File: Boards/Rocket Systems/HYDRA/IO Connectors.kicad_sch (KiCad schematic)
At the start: 0 parts

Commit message: IO connectors
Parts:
- added DSUB1: ~, HDL15-SL-B:HDL15-SL-B, symbol HDL15-SL-B:HDL15-SL-B
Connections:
- new net ACT_N2 OUT: DSUB1.14
- new net ACT_N2 PWR: DSUB1.15
- new net ACT_N2O OUT: DSUB1.10
- new net ACT_N2O PWR: DSUB1.11
- new net Extra Valve OUT: DSUB1.2
- new net Extra Valve PWR: DSUB1.3
- new net GND: DSUB1.1
- new net QuickDisco N2 OUT: DSUB1.6
- new net QuickDisco N2 PWR: DSUB1.7
- new net QuickDisco N2O OUT: DSUB1.4
- new net QuickDisco N2O PWR: DSUB1.5
- new net VENT_N2 OUT: DSUB1.12
- new net VENT_N2 PWR: DSUB1.13
- new net VENT_N2O OUT: DSUB1.8
- new net VENT_N2O PWR: DSUB1.9

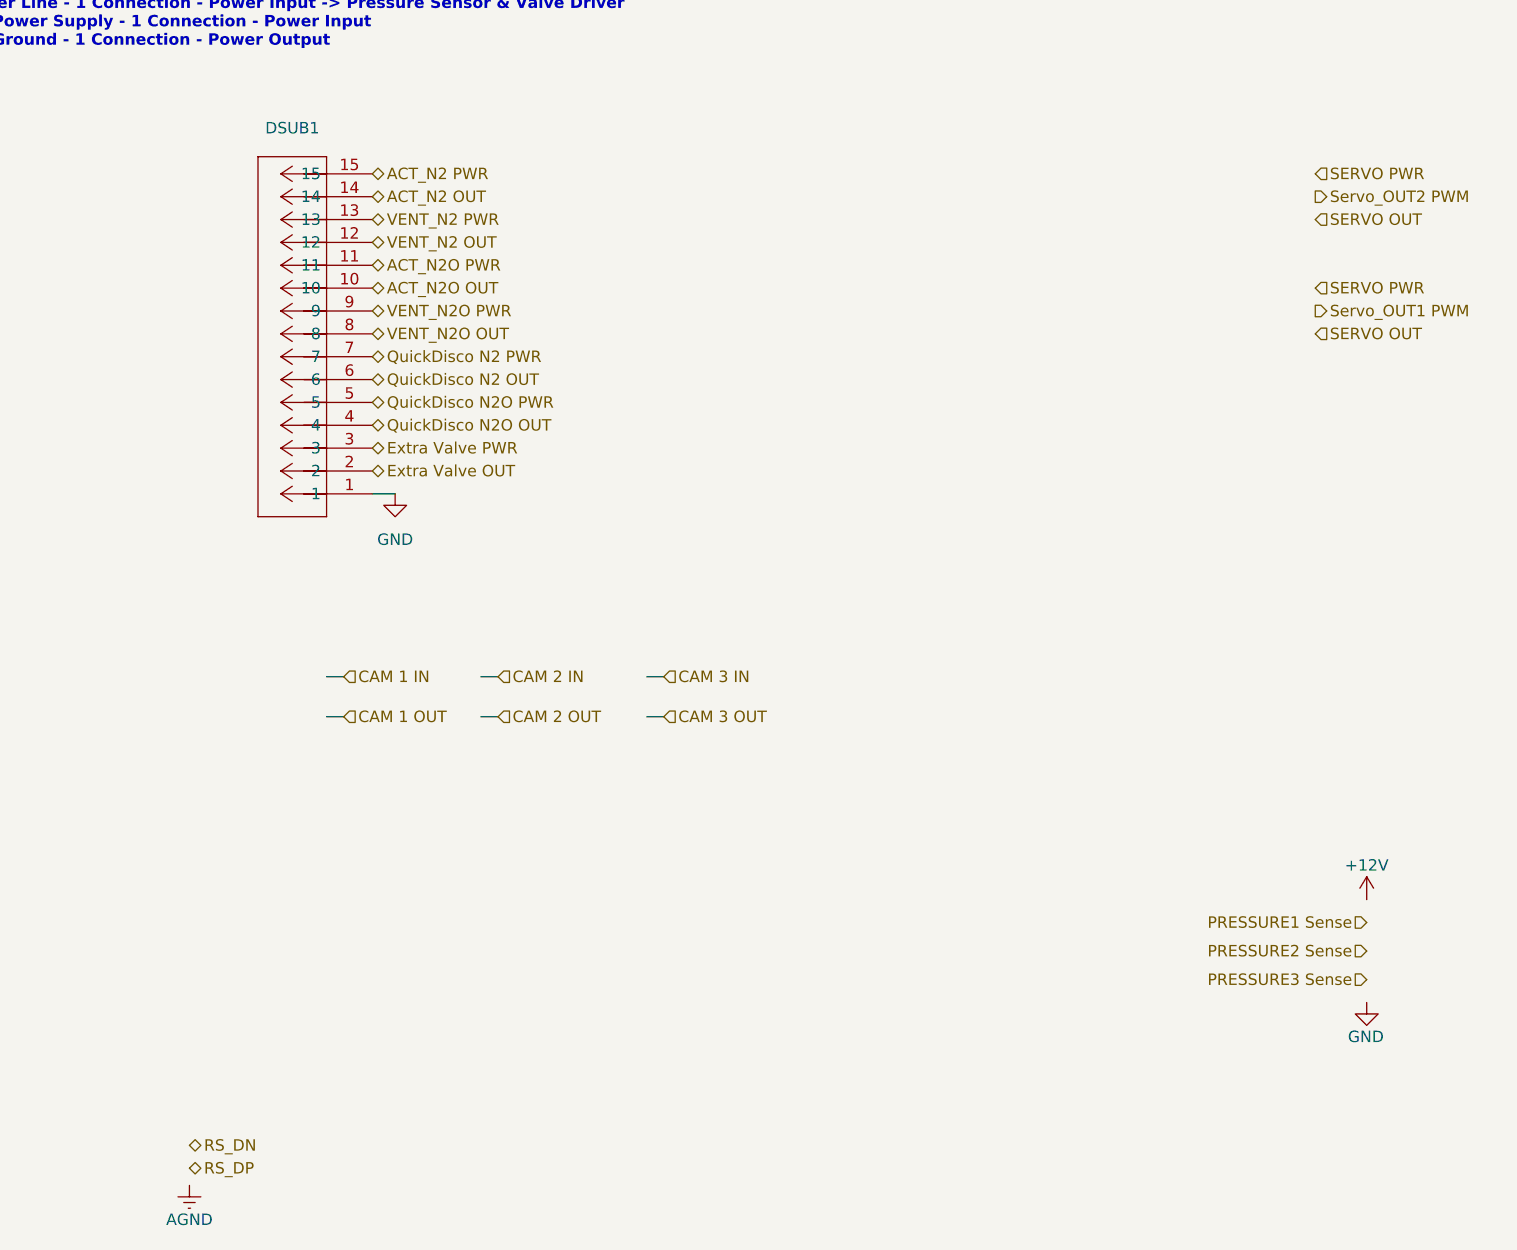
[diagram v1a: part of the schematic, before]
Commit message: bessels filter - anti aliasing
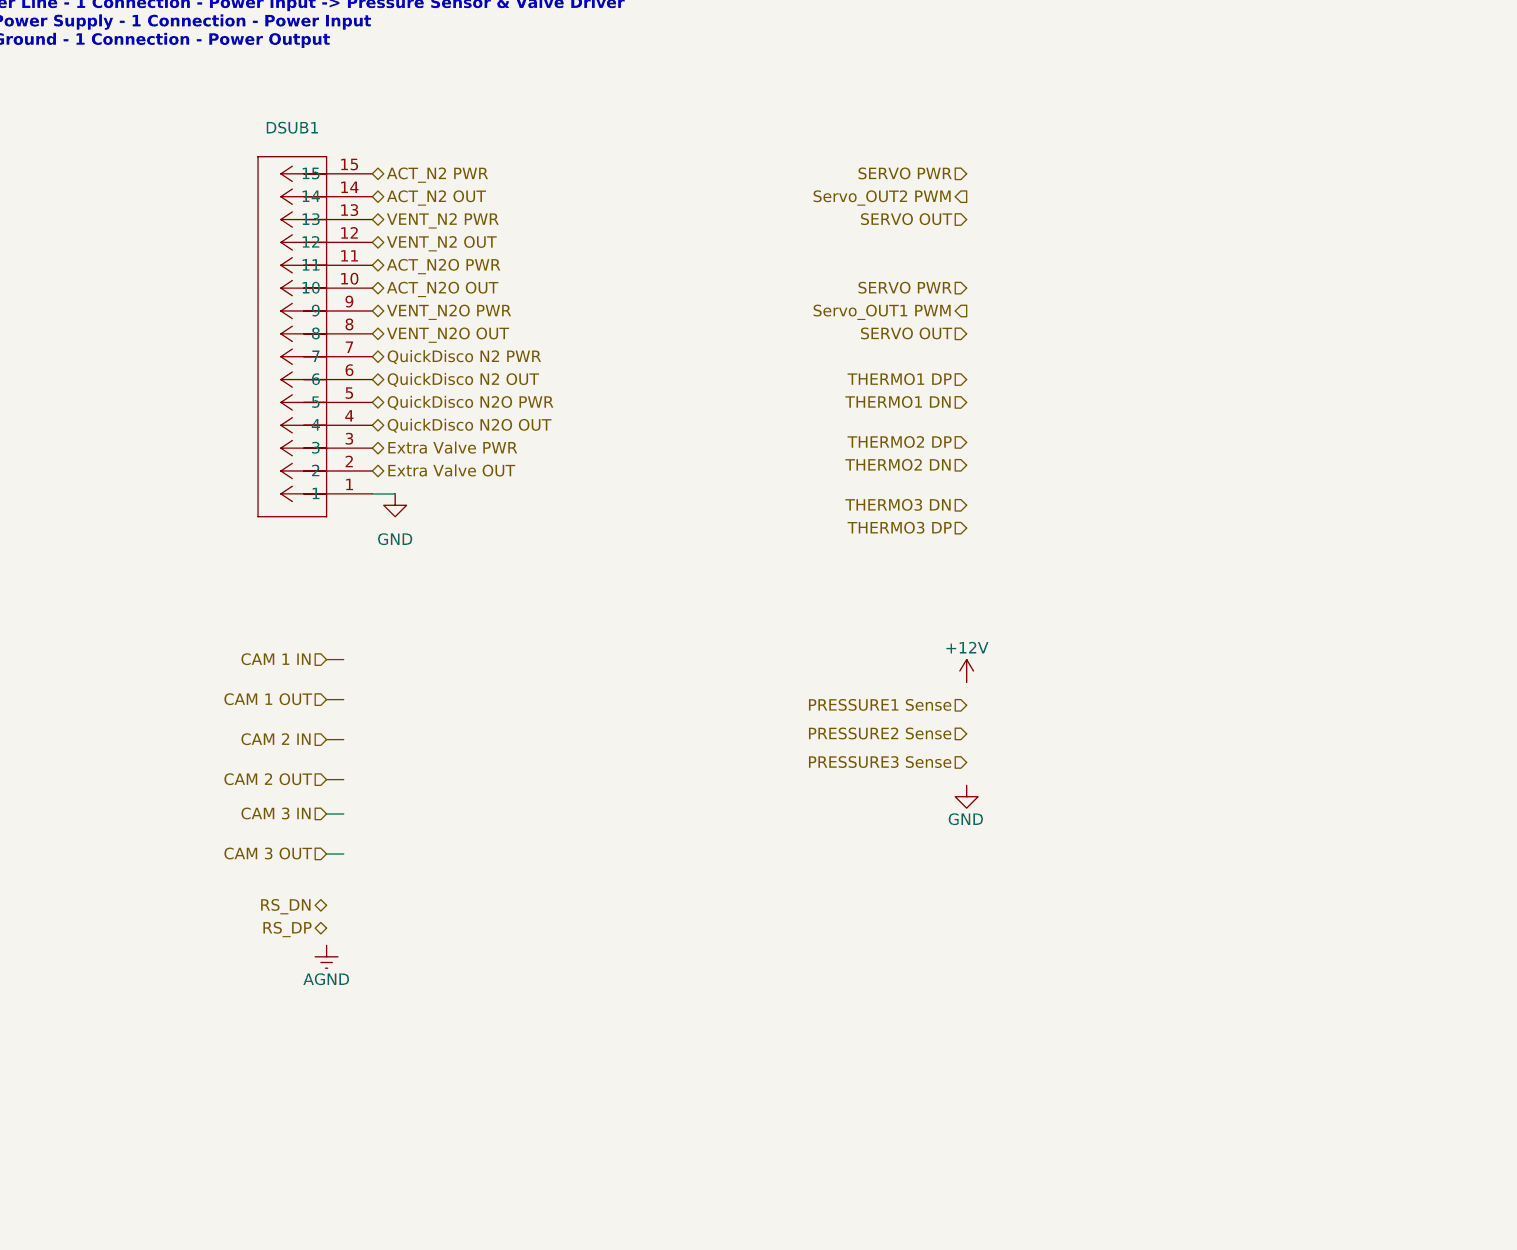
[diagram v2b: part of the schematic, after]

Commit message: HYDRA Schematic Update Final Touches
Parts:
- added H1, H3, H4: MountingHole, MountingHole:MountingHole_3.2mm_M3_ISO7380, symbol Mechanical:MountingHole
- added H2: MountingHole_Pad, MountingHole:MountingHole_3.2mm_M3_ISO7380_Pad, symbol Mechanical:MountingHole_Pad
- added J3, J4: XT30UPB-F, XT30UPB-F:XT30UPBF, symbol XT30UPB-F:XT30UPB-F
- added J5, J7: 5024430270, CONN_502443-02xx_MOL, symbol 5024430270:5024430270
- added J6: 5024430570, CONN_502443-05xx_MOL, symbol 5024430570:5024430570
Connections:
- net +12V: now also J6.1
- net AGND: now also H2.1
- net GND: now also J6.5
- net PRESSURE1 Sense: now also J6.2
- net PRESSURE2 Sense: now also J6.3
- net PRESSURE3 Sense: now also J6.4
- net RS_DN: now also J5.1
- net RS_DP: now also J5.2
- net SERVO OUT: now also J4.1
- net SERVO PWR: now also J4.2
- net Servo_OUT1 PWM: now also J7.1
- net Servo_OUT2 PWM: now also J7.2
- new net CAM IN: J3.2
- new net CAM OUT: J3.1
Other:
- moved on the sheet: DSUB1

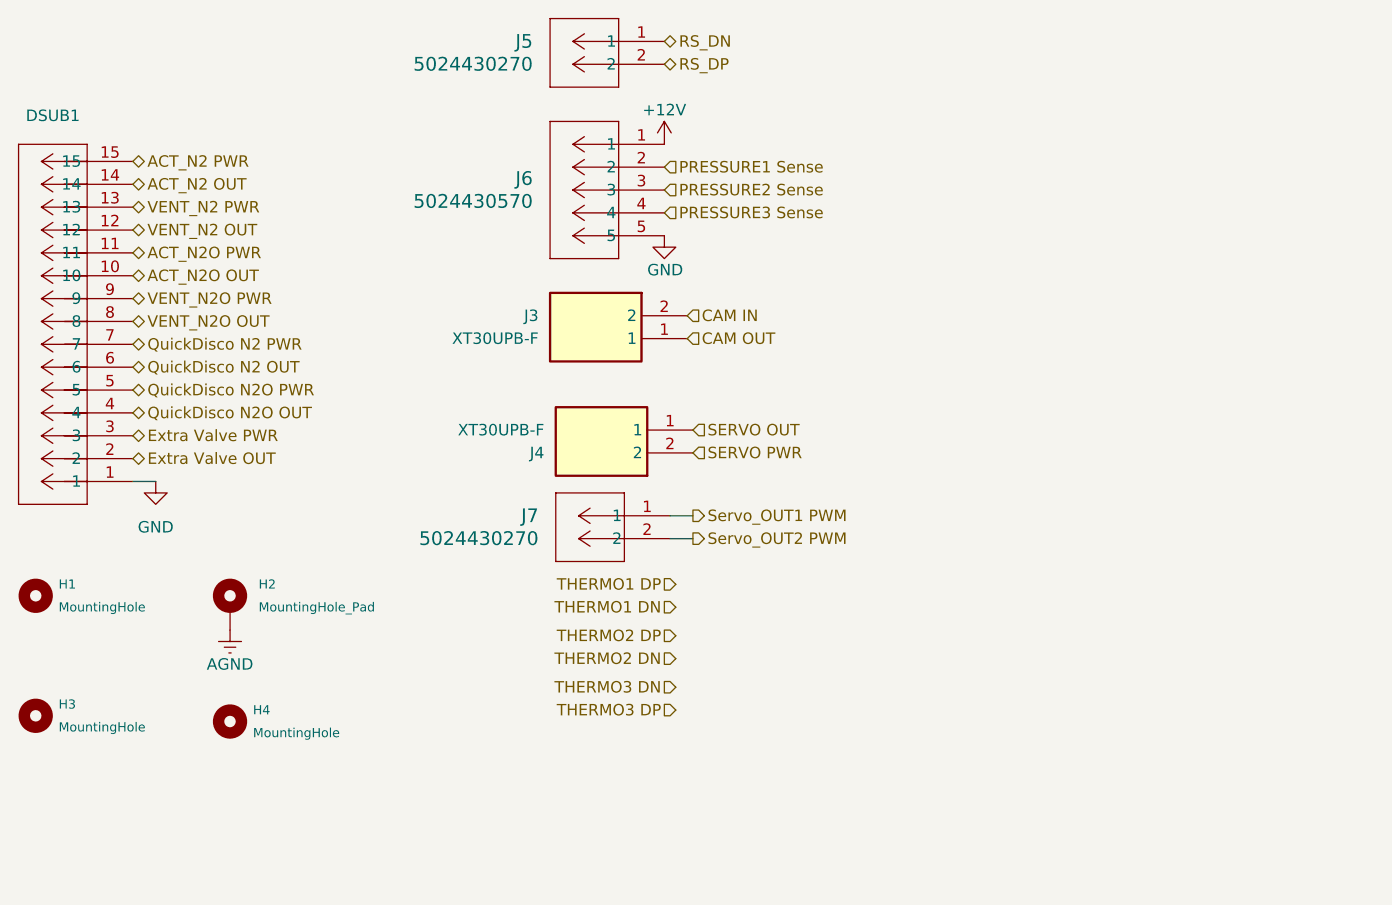
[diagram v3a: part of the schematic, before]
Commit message: HYDRA schematic pinout update pt1
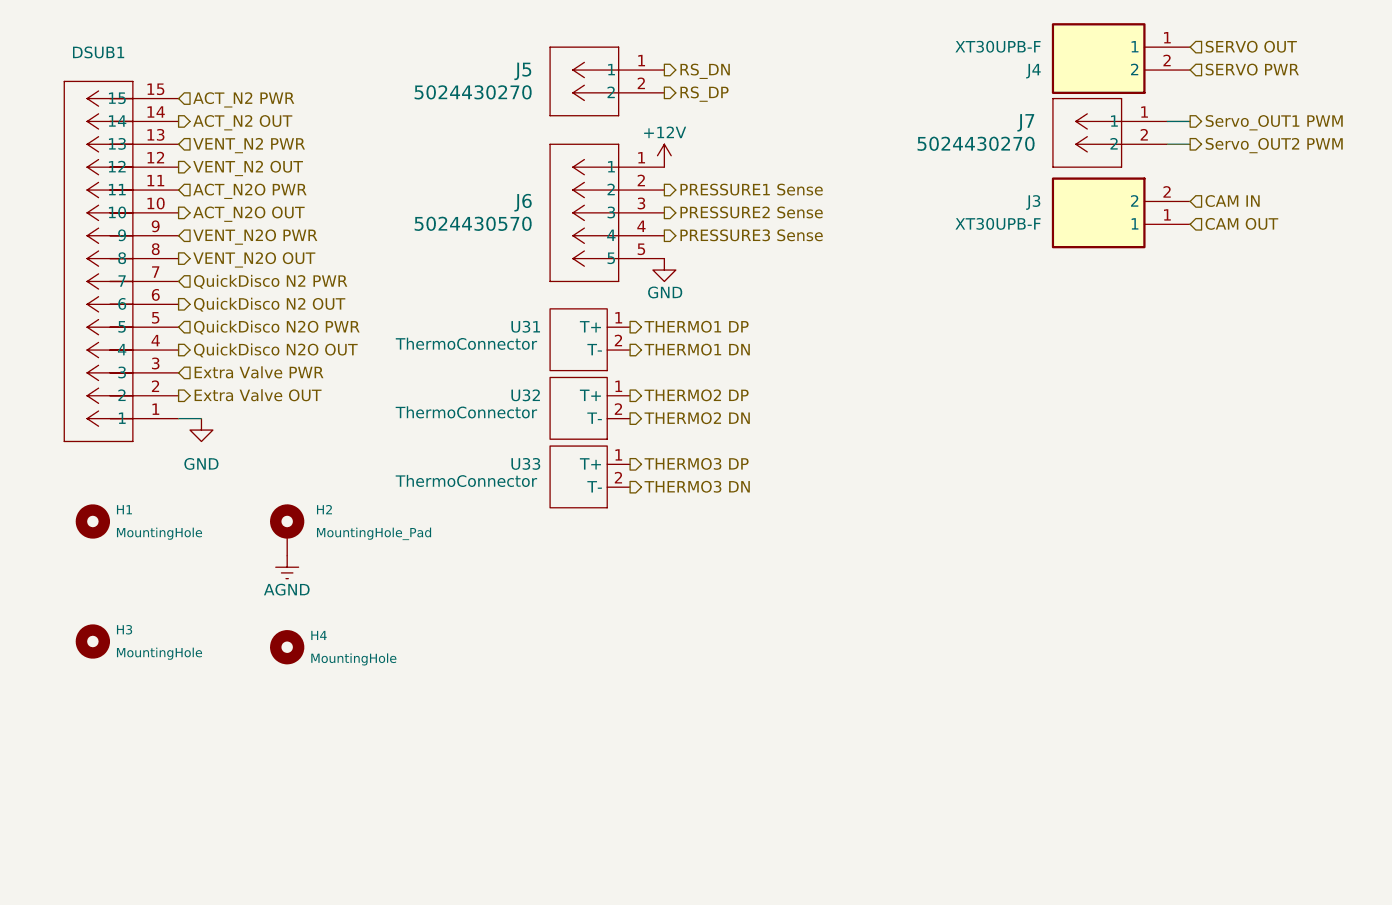
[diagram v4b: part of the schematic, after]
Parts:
- added U31, U32, U33: ThermoConnector, ThermoPCBConnector:Thermo Type K PCB Connector, symbol ThermoPCBConnector:ThermoPCBConnector
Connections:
- net THERMO1 DN: now also U31.2 (T-)
- net THERMO1 DP: now also U31.1 (T+)
- net THERMO2 DN: now also U32.2 (T-)
- net THERMO2 DP: now also U32.1 (T+)
- net THERMO3 DN: now also U33.2 (T-)
- net THERMO3 DP: now also U33.1 (T+)
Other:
- moved on the sheet: DSUB1, H1, H2, H3, H4, J3, J4, J5, J6, J7

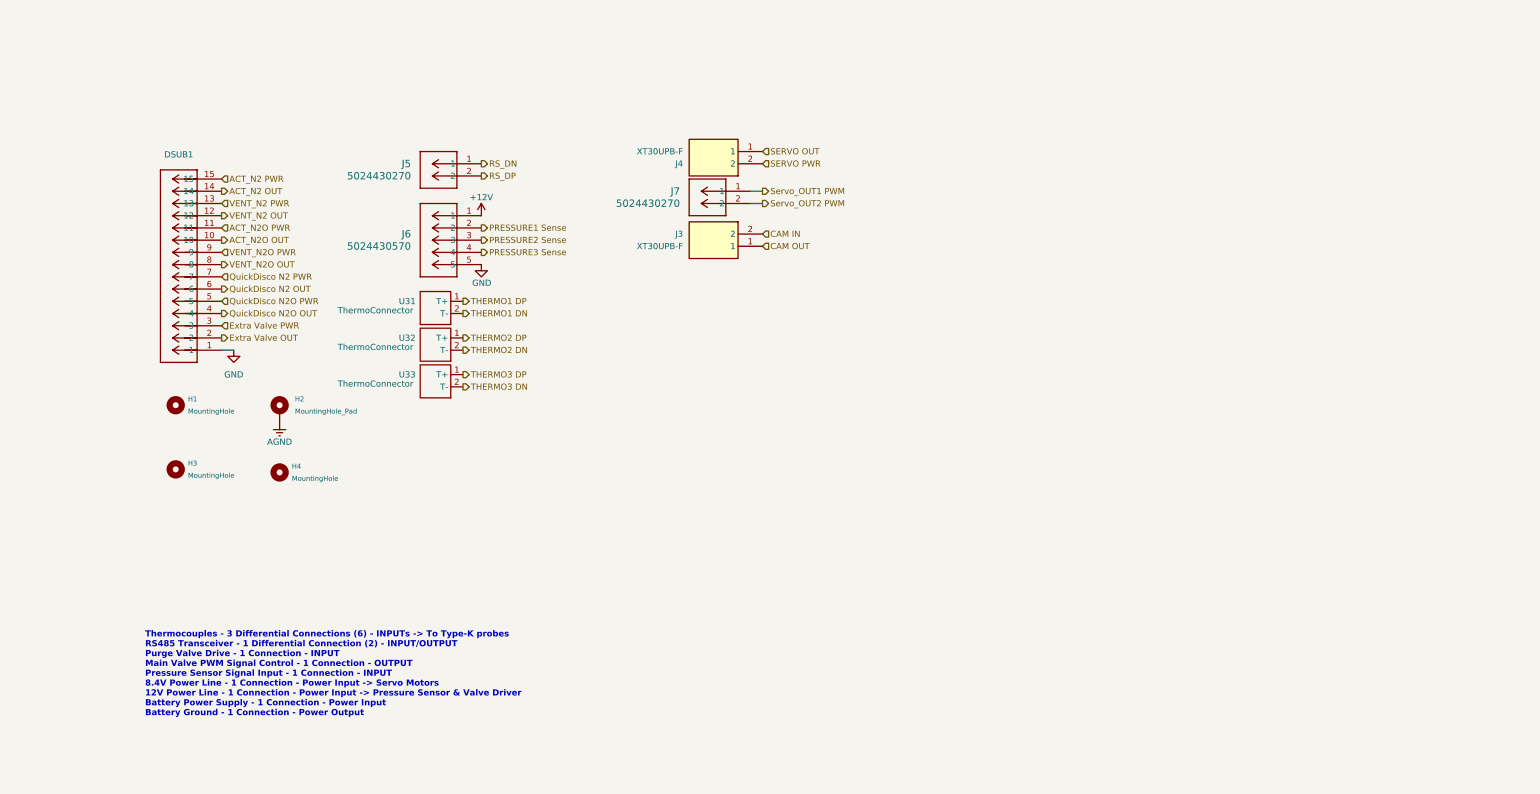
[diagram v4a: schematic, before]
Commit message: HYDRA schematic update, ELYTRA FULL REWORK
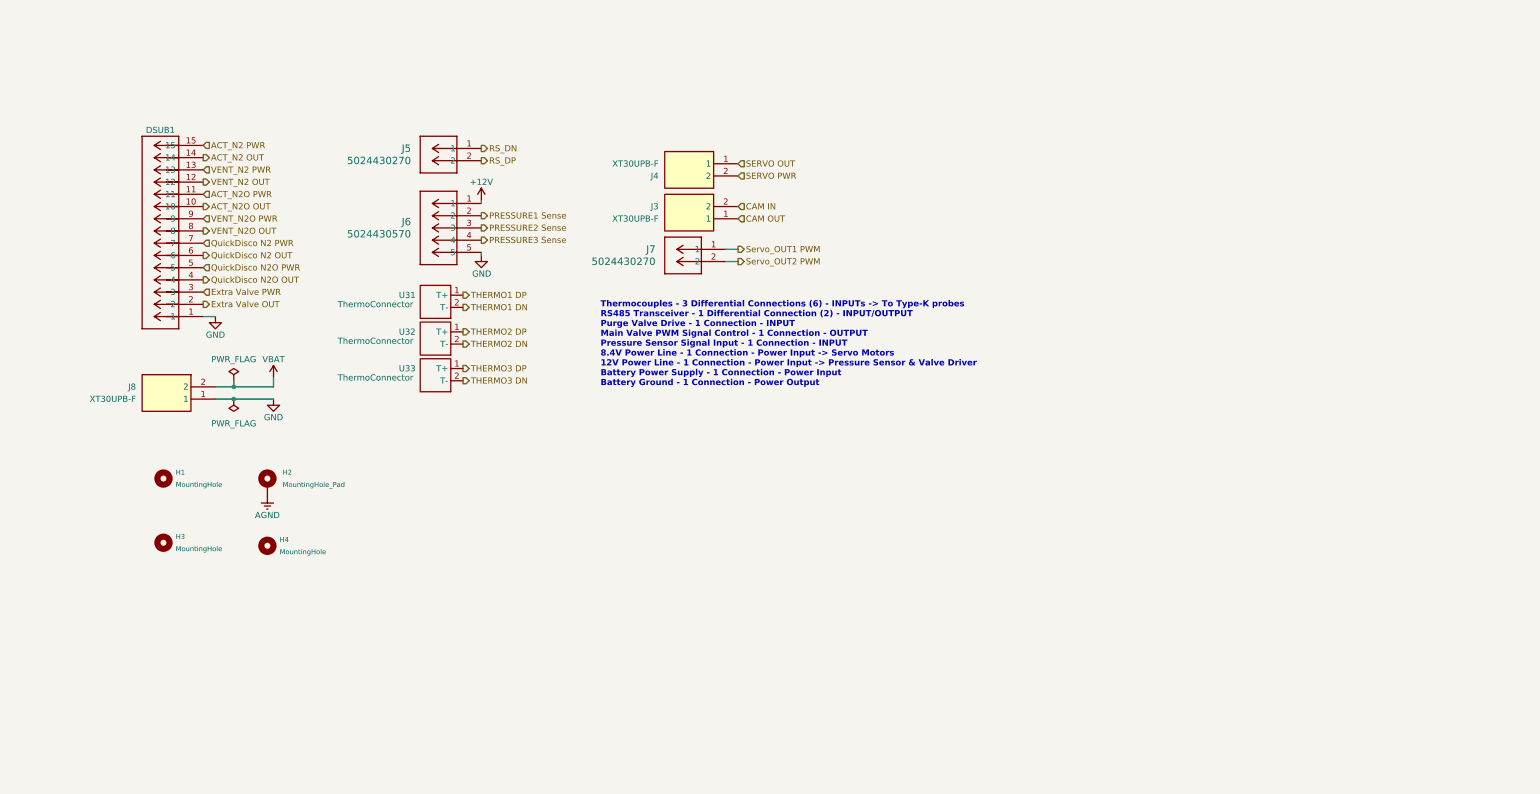
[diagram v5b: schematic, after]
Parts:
- added J8: XT30UPB-F, XT30UPB-F:XT30UPBF, symbol XT30UPB-F:XT30UPB-F
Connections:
- net GND: now also J8.1
- new net VBAT: J8.2
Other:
- moved on the sheet: DSUB1, H1, H2, H3, H4, J3, J4, J5, J6, J7, U31, U32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
